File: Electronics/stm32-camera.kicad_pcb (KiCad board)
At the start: 4 copper layers, 36 x 36 mm, 59 parts, among them CON1 MOLEX_47309-2651, P1 HEADER_MALE_2MM_01X06, P2 MOLEX_PICO_PTH_VERT_2_WAY, Q1 VEMT3700, U1 STM32F429VET6, U2 AP2210K-ADJ, U3 AP2210K-ADJ, U4 AP2210K-ADJ, U5 OV02640-VL9A, X1 CSTCE16M0V53A, X2 SWD

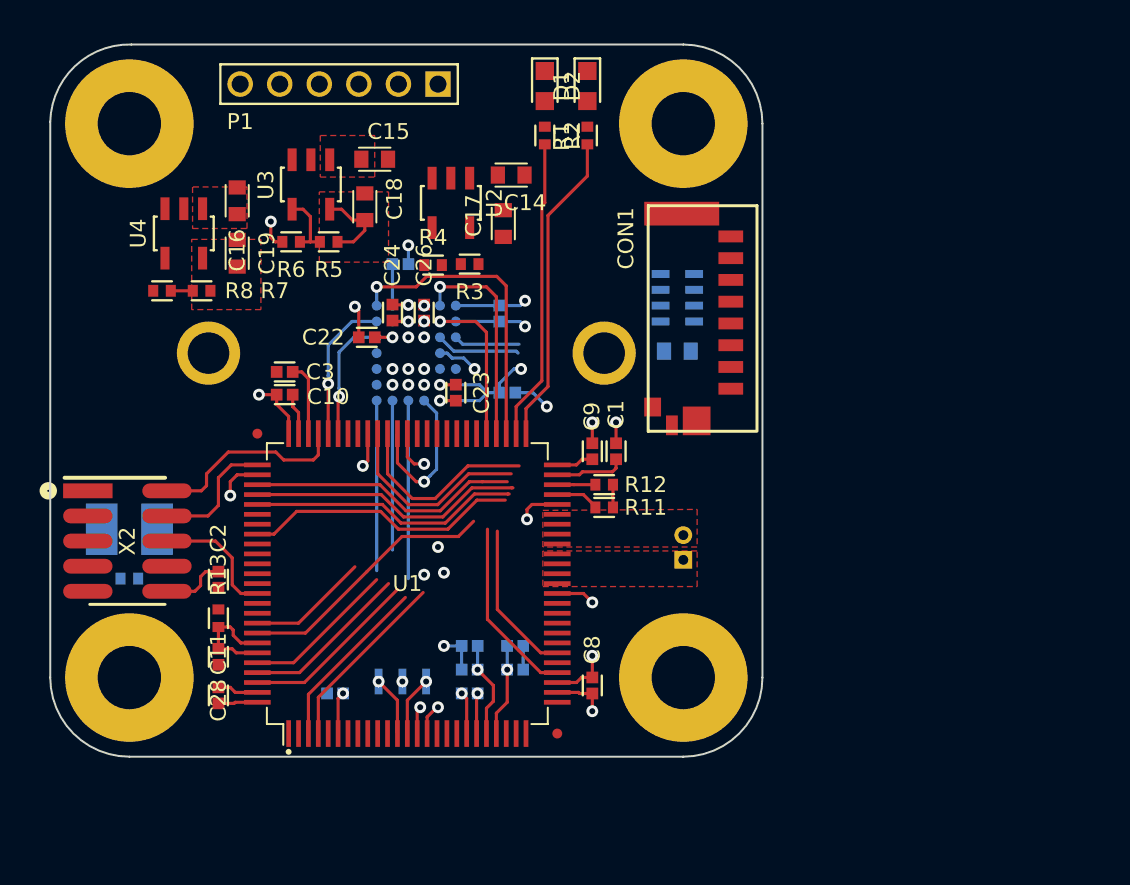
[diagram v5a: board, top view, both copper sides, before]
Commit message: Update with minor routing changes from laptop
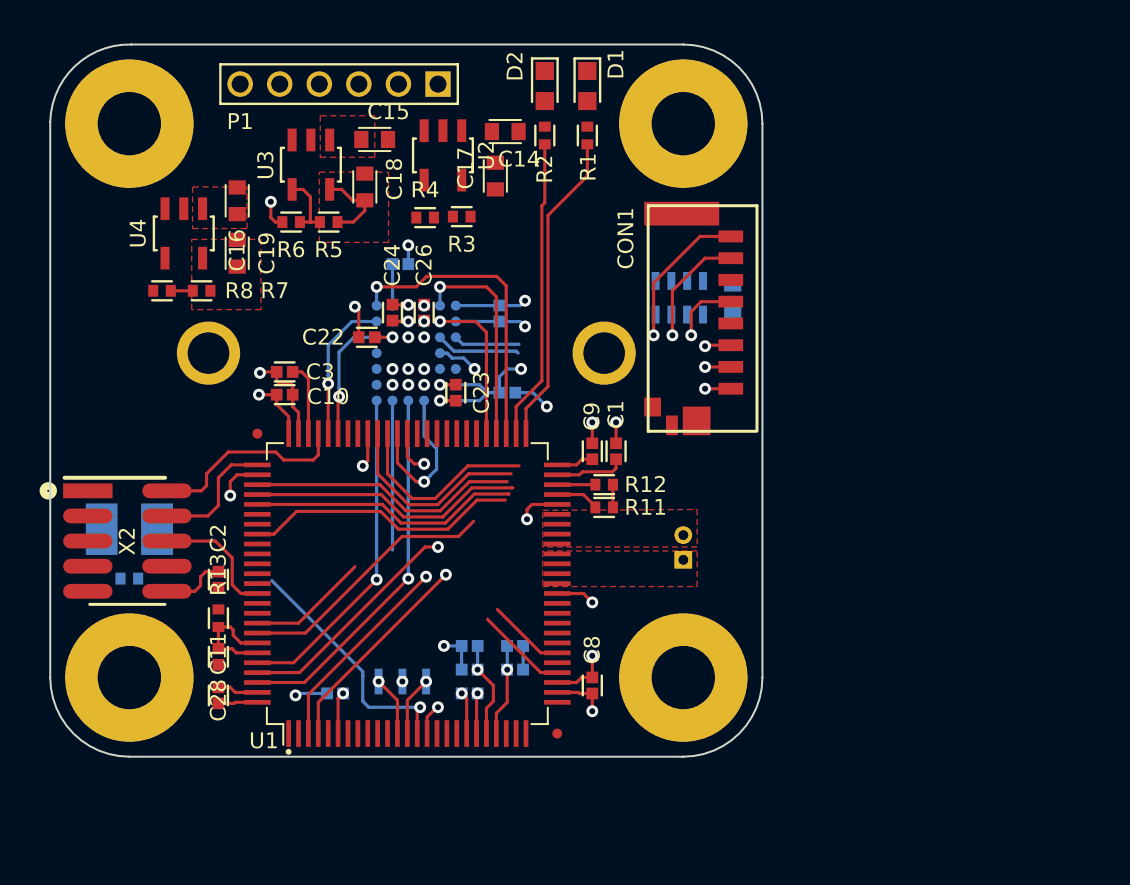
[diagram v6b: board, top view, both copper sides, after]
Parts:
- moved C20 3.89 mm to (134.5, 112.8), turned to 90 degrees
- moved U2 2.43 mm to (119.9, 105.6)
- moved R4 2.43 mm to (119.0, 108.8)
- moved C17 2.43 mm to (122.5, 106.7)
- moved R3 2.43 mm to (120.8, 108.7)
- moved C14 2.22 mm to (123.0, 104.4)
- moved C15 1.00 mm to (116.4, 104.8)
- moved C18 1.00 mm to (115.9, 107.2)
- moved R5 1.00 mm to (114.1, 109.0)
- moved R6 1.00 mm to (112.2, 109.0)
- moved U3 1.00 mm to (113.2, 106.1)
- moved R9 0.10 mm to (131.8, 112.8), turned to 270 degrees
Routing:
- net NRST: track 4.67 -> 15.7 mm
- net MICROSD_D1: track 10.1 -> 17.6 mm, vias 0 -> 1
- net PIXCK: track 19.7 -> 12.9 mm
- net MICROSD_D0: track 9.88 -> 15.8 mm, vias 0 -> 1
- net HREF: track 22.3 -> 17.7 mm
- net GND: track 27.5 -> 31.8 mm, vias 16 -> 18
- net MICROSD_CK: track 13.7 -> 17.1 mm, vias 0 -> 1
- net D2: track 17.3 -> 20.6 mm
- net D4: track 20.5 -> 22.1 mm
- net D6: track 19.9 -> 21.4 mm
- net MICROSD_CMD: track 14.0 -> 15.3 mm, vias 0 -> 1
- net MICROSD_D2: track 13.8 -> 15.1 mm, vias 0 -> 1
- net MICROSD_D3: track 14.0 -> 15.3 mm, vias 0 -> 1
- net D3: track 18.0 -> 18.8 mm, vias 0 -> 1
- net D7: track 16.4 -> 16.8 mm, vias 0 -> 1

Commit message: Footprint changes, using 0805 phototransistor now. Using different headers. Added flash header output. Moved parts around again, silkscreen changes, cosmetics. Routing etc.
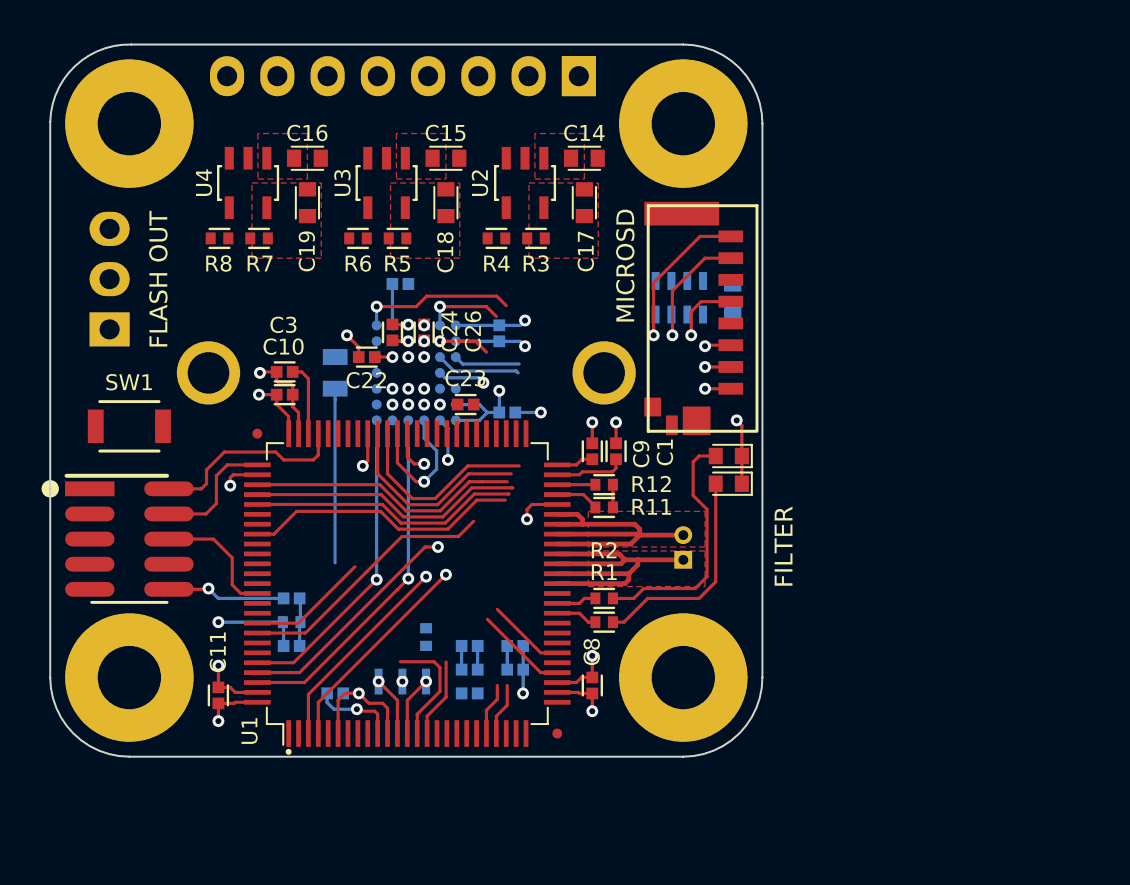
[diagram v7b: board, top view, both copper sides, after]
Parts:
- added P3: CONN_01X03, Applidyne_Header:Pin_Header_Straight_1x03, B.Cu at (103.0, 114.4)
- added SW1: B3U-1000P_SPST-NO_SMD, Applidyne_Switch:B3U-1000P, F.Cu at (104.0, 119.3)
- C2, C28, R13: moved to B.Cu
- D1, D2: footprint Applidyne_LED:LEDC1608X80L40N -> Applidyne_LED:LEDC1608X80L40L
- P1: value HEADER_MALE_2MM_01X06 -> CONN_01X08; footprint Applidyne_Connector:HDRV6W50P200_6X1_1200X200H400 -> Applidyne_Header:Socket_Strip_Straight_1x08; moved to B.Cu
- Q1: value VEMT3700 -> TEMT7000X01; footprint Applidyne_Device:VISHAY_VEMT3700N -> Applidyne_Special:TEMT7000X
- moved R1 24.6 mm to (128.0, 129.2), turned to 0 degrees
- moved R2 23.6 mm to (128.0, 128.0), turned to 0 degrees
- moved D1 21.3 mm to (134.3, 122.2), turned to 180 degrees
- moved D2 20.9 mm to (134.3, 120.8), turned to 180 degrees
- moved R10 15.3 mm to (119.0, 130.0), turned to 270 degrees
- moved Q1 13.1 mm to (114.4, 116.6), turned to 90 degrees
- moved P1 7.13 mm to (126.7, 101.6)
- moved C17 4.70 mm to (127.0, 108.0)
- moved U2 4.38 mm to (124.0, 107.0)
- moved C19 4.37 mm to (113.0, 108.0)
- moved C14 4.22 mm to (127.0, 105.8)
- moved C18 4.18 mm to (120.0, 108.0)
- moved C16 4.15 mm to (113.0, 105.8), turned to 0 degrees
- moved U4 4.13 mm to (110.0, 107.0)
- moved U3 3.94 mm to (117.0, 107.0)
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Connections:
- U1 pad 30: (no net) -> FLASH_DAC
- U1 pad 35: (no net) -> STATUS0
- U1 pad 36: (no net) -> STATUS1
- U1 pad 51: STATUS0 -> (no net)
- U1 pad 52: STATUS1 -> (no net)
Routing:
- net IRCUT_A: track 0.00 -> 18.5 mm
- net IRCUT_B: track 0.00 -> 16.9 mm
- net STATUS0: track 15.9 -> 2.11 mm
- net STATUS1: track 15.2 -> 2.03 mm
- net Net-(D2-PadA): track 0.00 -> 12.6 mm
- net AMBIENT_LIGHT: track 1.59 -> 12.8 mm, vias 1 -> 0
- net Net-(D1-PadA): track 0.00 -> 11.0 mm
- net D5: track 13.7 -> 6.11 mm
- net STROBE: track 15.4 -> 7.92 mm
- net PWDN: track 7.42 -> 0.00 mm, vias 1 -> 0
- net VSYNC: track 23.0 -> 15.7 mm
- net EXPSTB: track 10.9 -> 4.01 mm
- net RESET: track 6.35 -> 0.00 mm, vias 1 -> 0
- net HREF: track 17.7 -> 11.6 mm
- net FREX: track 7.70 -> 2.58 mm
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- added copper zone on F.Cu, net +3.3V
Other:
- board text added: "FILTER"
- board text added: "FLASH OUT"
- board text added: "MICROSD"

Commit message: Routing
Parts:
- moved R10 9.92 mm to (117.8, 139.8)
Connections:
- U1 pad 51: (no net) -> STROBE
- U1 pad 52: (no net) -> EXPSTB
- U1 pad 53: STROBE -> FREX
- U1 pad 54: EXPSTB -> (no net)
- U1 pad 55: FREX -> (no net)
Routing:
- net GND: track 35.6 -> 52.0 mm, vias 16 -> 21
- net MICROSD_DETECT: track 2.13 -> 14.4 mm, vias 1 -> 2
- net STROBE: track 7.92 -> 17.7 mm, vias 1 -> 2
- net SIO_D: track 5.27 -> 14.8 mm, vias 0 -> 1
- net PIXCK: track 9.03 -> 18.5 mm, vias 1 -> 2
- net PWDN: track 0.00 -> 9.35 mm, vias 0 -> 1
- net SIO_C: track 6.50 -> 15.8 mm, vias 0 -> 1
- net PWR_EN: track 1.83 -> 10.8 mm, vias 1 -> 3
- net RESET: track 0.00 -> 8.91 mm, vias 0 -> 1
- net D5: track 6.11 -> 14.9 mm, vias 0 -> 1
- net NRST: track 11.9 -> 20.5 mm, vias 1 -> 2
- net VSYNC: track 15.7 -> 24.1 mm, vias 1 -> 2
- net HREF: track 11.6 -> 19.4 mm, vias 1 -> 2
- net EXPSTB: track 4.01 -> 10.5 mm
- net +3.3V: track 35.3 -> 41.1 mm, vias 6 -> 8
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- added copper zone on F.Cu, net GND
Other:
- board text removed: "FILTER"
